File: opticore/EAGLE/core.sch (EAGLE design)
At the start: 121 parts, among them IC1 MCP1825S-3302E, IC2 MC33269T-5.0, J1 POWER_JACKSLT, Q1 MMDT3904, Q2 2N3904, Q3 2N3904, Q4 2N3904, Q5 2N3904, Q6 2N3904, Q7 2N3904, Q8 2N3904, U2 STM32F10XCXT6, U3 SST25VF040B-S2, U4 NL17SZ125SOT553, X1 USB-MICROB, X2 IPEX-20279-001E, Y1 32Khz, Y2 8Mhz

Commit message: Initial placement of relays
Still need to do a lot of work. Placement is temporary.

LEDs and the rest of the components need to be placed.

One problem is that I can't move what they originally did. Option #1: Redo what they did. (not happening) Option #2: Try adding their schematic as a part then placing it on a new shm. Option #3: Try to find a way to move it online.

Signed-off-by: Scott Lerner <scottphiliplerner@gmail.com>
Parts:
- removed Q1: MMDT3904, SparkFun-DiscreteSemi:MMDT3904
- removed U$1: SPARK_LOGO2, Spark:SPARK_LOGO2
- added Q9: 2N3904, transistor-npn:2N3904
- Q2: value 2N3904 -> MMDT3904; device transistor-npn:2N3904 -> SparkFun-DiscreteSemi:MMDT3904
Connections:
- net +3V3: now also Q2G$1.C; no longer Q1G$1.C
- net GND: now also Q2G$2.E, Q9.E; no longer Q1G$2.E, Q2.E
- net N$13: now also Q2G$1.B, Q2G$2.C; no longer Q1G$1.B, Q1G$2.C
- net N$16: now also Q2G$1.E; no longer Q1G$1.E
- net N$18: now also Q3.C; no longer Q2.C
- net N$19: now also Q4.C; no longer Q3.C
- net N$20: now also Q4.B; no longer Q3.B
- net N$22: now also Q6.C; no longer Q4.C
- net N$23: now also Q6.B; no longer Q4.B
- net N$24: now also Q3.B; no longer Q2.B
- net N$26: now also Q7.C; no longer Q5.C
- net N$27: now also Q7.B; no longer Q5.B
- net N$29: now also Q5.C; no longer Q6.C
- net N$30: now also Q5.B; no longer Q6.B
- net N$32: now also Q8.C; no longer Q7.C
- net N$33: now also Q8.B; no longer Q7.B
- net N$35: now also Q9.C; no longer Q8.C
- net N$36: now also Q9.B; no longer Q8.B
- net N$8: now also Q2G$2.B; no longer Q1G$2.B
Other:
- moved on the sheet: Q3, Q4, Q5, Q6, Q7, Q8

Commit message: Close to final revision
I'm working on laying down the final placement as well as the ground
planes. I'll try and work on it soon.
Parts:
- removed ANT1: AT8010, Spark:AT8010
- removed BTN, RESET: KMR211GLFS, Spark:TAC_SWITCHSMD
- removed C1, C2: 4.7uF, rcl:C-EUC0603
- removed C10, C11: 22pF, rcl:C-EUC0603
- removed C12, C13, C14, C16, C3, C6, C7: 100nF, rcl:C-EUC0603
- removed C15: 10uF, Spark:TANT-CAP1206
- removed C4: 2.2pF, rcl:C-EUC0603
- removed C5, C8, C9: 10pF, rcl:C-EUC0603
- removed D8: 1N4004, diode:1N4004
- removed D9: GREEN, SparkFun-LED:LED-GREEN0603
- removed IC1: MCP1825S-3302E, Spark:MCP1825S-SOT223
- removed JP1, JP2: M12PTH, Spark:M12PTH
- removed JP3, JP4, JP5, JP6, JP7, JP8, JP9: (no value), SparkFun-Connectors:M03-SCREW-5MM
- removed L1: 2.2nH, SparkFun-Passives:INDUCTOR0603
- removed L2: Bead, SparkFun-Passives:INDUCTOR0603
- removed LED_RGB: (no value), Spark:TOPLED-3PLCC
- removed LED_USR: (no value), SparkFun:LED0603
- removed LOGO1: OSHW-LOGOS, SparkFun-Aesthetics:OSHW-LOGOS
- removed Q8, Q9: 2N3904, transistor-npn:2N3904
- removed R25, R27, R28, R30: 1K, SparkFun-Passives:RESISTOR0402-RES
- removed R26, R29: 10K, SparkFun-Passives:RESISTOR0402-RES
- removed R31: 1K, SparkFun-Passives:RESISTORAXIAL-0.3
- removed R32, R33: 4.7K, SparkFun-Passives:RESISTOR0402-RES
- removed RN1: EXB-38V102JV, resistor-dil:4R-NEXB38V
- removed STANDOFF1, STANDOFF2, STANDOFF3: STAND-OFF, SparkFun-Electromechanical:STAND-OFF
- removed U1: (no value), CC3000:CC3000
- removed U2: STM32F10XCXT6, stm32:STM32F10XCXT6
- removed U3: SST25VF040B-S2, Spark:SST25VF040B-S2
- removed U4: NL17SZ125SOT553, Spark:NL17SZ125SOT553
- removed X2: IPEX-20279-001E, Spark:IPEX-20279-001E
- removed Y1: 32Khz, Spark:Q_FC135
- removed Y2: 8Mhz, SparkFun-FreqCtrl:CRYSTAL5X3
- added JP11, JP12: M12PTH, Spark:M12PTH
- added LED8: (no value), SparkFun-LED:LED3MM
- added LOGO2: OSHW-LOGOL, SparkFun-Aesthetics:OSHW-LOGOL
- added Q1: 2N3904, transistor-npn:2N3904
- C17, C18, C19: value (none) -> 100uF
- D1: value DIODE -> 1N4004; device Spark:DIODE -> diode:1N4004
- LED1, LED2, LED3, LED4, LED5, LED6, LED7: value RED -> (none); device SparkFun-LED:LED0603 -> SparkFun-LED:LED3MM
- Q2: value MMDT3904 -> 2N3904; device SparkFun-DiscreteSemi:MMDT3904 -> transistor-npn:2N3904
- R1, R8: value 10K -> 1K; device rcl:R-US_R0603 -> SparkFun-Resistors:RESISTORAXIAL-0.3
- R10, R13, R16, R19, R24: device SparkFun-Passives:RESISTOR0402-RES -> SparkFun-Resistors:RESISTORAXIAL-0.3
- R11, R14, R17, R20: value 10K -> 1K; device SparkFun-Passives:RESISTOR0402-RES -> SparkFun-Resistors:RESISTORAXIAL-0.3
- R12, R15, R18, R21: value 1K -> 10K; device SparkFun-Passives:RESISTOR0402-RES -> SparkFun-Resistors:RESISTORAXIAL-0.3
- R2: value 33K -> 1K; device rcl:R-US_R0603 -> SparkFun-Resistors:RESISTORAXIAL-0.3
- R22: value 1K -> 4.7K; device SparkFun-Passives:RESISTOR0402-RES -> SparkFun-Resistors:RESISTORAXIAL-0.3
- R23: value 10K -> 4.7K; device SparkFun-Passives:RESISTOR0402-RES -> SparkFun-Resistors:RESISTORAXIAL-0.3
- R3: value 1K5 -> 10K; device rcl:R-US_R0603 -> SparkFun-Resistors:RESISTORAXIAL-0.3
- R4: device rcl:R-US_R0603 -> SparkFun-Resistors:RESISTORAXIAL-0.3
- R5: value 22 -> 1K; device rcl:R-US_R0603 -> SparkFun-Resistors:RESISTORAXIAL-0.3
- R6: value 22 -> 10K; device rcl:R-US_R0603 -> SparkFun-Resistors:RESISTORAXIAL-0.3
- R7: value 47K -> 1K; device rcl:R-US_R0603 -> SparkFun-Resistors:RESISTORAXIAL-0.3
- R9: value 1K -> 10K; device rcl:R-US_R0603 -> SparkFun-Resistors:RESISTORAXIAL-0.3
- X1: value USB-MICROB -> FFKV8; device Spark:USBUSB-MICROB-SLOT-HOLE -> con-phoenix-508:FFKV8
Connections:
- removed net BTN: BTN.3, U2PORTB_L.PB2
- removed net LED1: LED_USR.A, RN1D.1
- removed net LED2: RN1A.2, U2PORTA_H.PA8
- removed net LED3: RN1B.2, U2PORTA_H.PA9
- removed net LED4: RN1C.2, U2PORTA_H.PA10
- removed net MAIN1: JP3.2, U$2.MAIN
- removed net MAIN2: JP4.2, U$4.MAIN
- removed net MAIN3: JP7.2, U$7.MAIN
- removed net MAIN4: JP5.2, U$5.MAIN
- removed net MAIN5: JP6.2, U$6.MAIN
- removed net MAIN6: JP8.2, U$8.MAIN
- removed net MAIN7: JP9.2, U$9.MAIN
- removed net MEM_CS: R9.1, U2PORTB_H.PB9, U3.CE
- removed net N$10: LED_RGB.CRED, RN1A.1
- removed net N$12: LED_RGB.CBLUE, RN1B.1
- removed net N$13: Q2G$1.B, Q2G$2.C, R1.1, R2.2
- removed net N$14: LED_RGB.CGREEN, RN1C.1
- removed net N$15: U1.SDA_CC3000, U1.SDA_EEPROM
- removed net N$16: Q2G$1.E, R3.2
- removed net N$17: LED2.A, R13.1
- removed net N$21: LED3.A, R16.1
- removed net N$25: LED4.A, R19.1
- removed net N$28: LED5.A, R22.1
- removed net N$31: LED6.A, R25.1
- removed net N$34: LED7.A, R28.1
- removed net N$43: R32.2, SJ1.3
- removed net N$44: R33.2, SJ1.1
- removed net NC1: JP3.3, U$2.NC
- removed net NC2: JP4.3, U$4.NC
- removed net NC3: JP7.3, U$7.NC
- removed net NC4: JP5.3, U$5.NC
- removed net NC5: JP6.3, U$6.NC
- removed net NC6: JP8.3, U$8.NC
- removed net NC7: JP9.3, U$9.NC
- removed net OSC32_IN: C9.1, U2PORTC.PC14, Y1.1
- removed net OSC32_OUT: C8.1, U2PORTC.PC15, Y1.2
- removed net OSC_IN: C11.1, U2PORTD/OSC.PD0/OSC<=, Y2.1
- removed net OSC_OUT: C10.1, U2PORTD/OSC.PD1/OSC=>, Y2.2
- removed net SPI_DOUT: U1.SPI_DOUT, U4.IN
- removed net SPI_MISO: U2PORTB_H.PB14, U3.SO, U4.OUT
- removed net SPI_MOSI: U1.SPI_DIN, U2PORTB_H.PB15, U3.SI
- removed net SPI_SCK: U1.SPI_CLK, U2PORTB_H.PB13, U3.SCK
- removed net USBM: R6.1, U2PORTA_H.PA11
- removed net USBP: R5.1, U2PORTA_H.PA12
- removed net USB_DISC: R4.1, R7.2, U2PORTB_H.PB10
- removed net UVCC: D1.ANODE, R1.2, X1.VBUS
- removed net WIFI_CS: U1.SPI_CS, U2PORTB_H.PB12, U4./OE
- removed net WIFI_EN: U1.VBAT_SW_EN, U2PORTB_H.PB8
- removed net WIFI_INT: U1.SPI_IRQ, U2PORTB_H.PB11
- new net MAIN: U$2.MAIN, U$4.MAIN, U$5.MAIN, U$6.MAIN, U$7.MAIN, U$8.MAIN, U$9.MAIN, X1-8.2
- net !RST: now also JP12.2; no longer C6.2, JP2.2, R8.1, RESET.1, U2RESET.NRST
- net +3V3: now also JP12.1; no longer C12.1, C14.1, C16.1, C2.1, C3.1, C7.1, IC1.OUT, JP2.1, L2.1, LED_RGB.A2, Q2G$1.C, R7.1, R8.2, R9.2, U1.VBAT_IN, U1.VIO_HOST, U2AN_POWER.VBAT, U2POWER.VDD_1, U2POWER.VDD_2, U2POWER.VDD_3, U3.HOLD, U3.VDD, U3.WP, U4.VCC
- net 5V: now also D1.C, R1.2, R24.1, R4.2, R7.2; no longer D8.C, R22.2, R25.2, R28.2, R31.1
- net A2: now also JP11.10; no longer JP1.10, U2PORTA_L.PA4
- net A3: now also JP11.9; no longer JP1.9, U2PORTA_L.PA5
- net A4: now also JP11.8; no longer JP1.8, U2PORTA_L.PA6
- net A5: now also JP11.7; no longer JP1.7, U2PORTA_L.PA7
- net A6: now also JP11.6; no longer JP1.6, U2PORTB_L.PB0
- net A7: now also JP11.5; no longer JP1.5, U2PORTB_L.PB1
- net D7: now also JP12.5; no longer JP2.5, RN1D.2, U2PORTA_H.PA13
- net GND: now also JP11.2, JP12.4, LED8.C, Q1.E, Q2.E, R12.1, R15.1, R18.1, R21.1, R3.1, R6.1, R9.1; no longer BTN.2, C1.2, C10.2, C11.2, C12.2, C13.2, C14.2, C15.-, C16.2, C2.2, C3.2, C6.1, C7.2, C8.2, C9.2, D9.C, IC1.GND@1, IC1.GND@2, JP1.2, JP2.4, L1.2, LED_USR.C, Q2G$2.E, Q8.E, Q9.E, R11.1, R14.1, R17.1, R2.1, R20.1, R23.1, R26.1, R29.1, RESET.4, U1.EXT_32K, U1.GND@1, U1.GND@10, U1.GND@11, U1.GND@16, U1.GND@18, U1.GND@20, U1.GND@22, U1.GND@25, U1.GND@31, U1.GND@32, U1.GND@33, U1.GND@34, U1.GND@36, U1.GND@37, U1.GND@38, U1.GND@39, U1.GND@40, U1.GND@41, U1.GND@42, U1.GND@43, U1.GND@44, U1.GND@45, U1.GND@46, U1.GND@9, U2AN_POWER.VSSA, U2POWER.VSS_1, U2POWER.VSS_2, U2POWER.VSS_3, U2RESET.BOOT0, U3.VSS, U4.GND, X1.GND, X2.GND@1
- net N$1: now also LED1.A, R1.1; no longer R3.1, R5.2, X1.D+
- net N$18: now also D1.A, Q1.C; no longer D2.A, Q3.C
- net N$19: now also D2.A, Q2.C; no longer D3.A, Q4.C
- net N$2: now also LED2.A, R4.1; no longer C5.2, X2.1
- net N$20: now also Q2.B, R5.2, R6.2; no longer Q4.B, R14.2, R15.1
- net N$22: now also D5.A, LED5.C, Q5.C; no longer D4.A, LED3.C, Q6.C
- net N$23: now also Q5.B, R14.2, R15.2; no longer Q6.B, R17.2, R18.1
- net N$24: now also Q1.B, R2.2, R3.2; no longer Q3.B, R11.2, R12.1
- net N$26: now also D6.A, LED6.C, Q6.C; no longer D5.A, LED4.C, Q7.C
- net N$27: now also Q6.B, R17.2, R18.2; no longer Q7.B, R20.2, R21.1
- net N$29: now also D3.A, LED3.C, Q3.C; no longer D6.A, LED5.C, Q5.C
- net N$3: now also LED5.A, R13.1; no longer ANT1.SIGNAL, C4.1, L1.1
- net N$30: now also Q3.B, R8.2, R9.2; no longer Q5.B, R23.2, R24.1
- net N$32: now also LED7.C, Q7.C; no longer LED6.C, Q8.C
- net N$33: now also Q7.B, R20.2, R21.2; no longer Q8.B, R26.2, R27.1
- net N$35: now also D4.A, LED4.C, Q4.C; no longer D8.A, LED7.C, Q9.C
- net N$36: now also Q4.B, R11.2, R12.2; no longer Q9.B, R29.2, R30.1
- net N$39: now also LED8.A, R24.2; no longer D9.A, R31.2
- net N$4: now also LED6.A, R16.1; no longer LED1.A, R10.1
- net N$5: now also LED3.A, R7.1; no longer C4.2, C5.1, U1.RF_ANT
- net N$6: now also LED4.A, R10.1; no longer R6.2, X1.D-
- net N$7: now also LED7.A, R19.1; no longer U1.SCL_CC3000, U1.SCL_EEPROM
- net N$8: now also R22.2, SJ1.3; no longer Q2G$2.B, R4.2
- net N$9: now also R23.2, SJ1.1; no longer U1.WL_EN1, U1.WL_EN2
- net NO1: now also X1-7.2; no longer JP3.1
- net NO2: now also X1-6.2; no longer JP4.1
- net NO3: now also X1-5.2; no longer JP7.1
- net NO4: now also U$9.NO, X1-4.2; no longer JP5.1, U$5.NO
- net NO5: now also U$5.NO, X1-3.2; no longer JP6.1, U$6.NO
- net NO6: now also U$6.NO, X1-2.2; no longer JP8.1, U$8.NO
- net NO7: now also U$8.NO, X1-1.2; no longer JP9.1, U$9.NO
- net RAW: now also JP11.1; no longer C1.1, D1.CATHODE, IC1.IN, JP1.1
- net RELAY1: now also JP12.12, R2.1; no longer JP2.12, R12.2, U2PORTB_L.PB7
- net RELAY2: now also JP12.11, R5.1; no longer JP2.11, R15.2, U2PORTB_L.PB6
- net RELAY3: now also JP12.10, R8.1; no longer JP2.10, R24.2, U2PORTB_L.PB5
- net RELAY4: now also JP12.9, R11.1; no longer JP2.9, R18.2, U2PORTB_L.PB4
- net RELAY5: now also JP12.8, R14.1; no longer JP2.8, R21.2, U2PORTB_L.PB3
- net RELAY6: now also JP12.7, R17.1; no longer JP2.7, R27.2, U2PORTA_H.PA15
- net RELAY7: now also JP12.6, R20.1; no longer JP2.6, R30.2, U2PORTA_H.PA14
- net RX: now also JP11.4; no longer JP1.4, U2PORTA_L.PA3
- net SCL: now also JP11.11, R23.1; no longer JP1.11, R33.1, U2PORTA_L.PA1
- net SDA: now also JP11.12, R22.1; no longer JP1.12, R32.1, U2PORTA_L.PA0
- net TX: now also JP11.3; no longer JP1.3, U2PORTA_L.PA2
- net VDDA: now also JP12.3; no longer C13.1, C15.+, JP2.3, L2.2, U2AN_POWER.VDDA
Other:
- note removed: "Arduino Pro Mini Design by Spark Fun Electronics"
- note removed: "External FLASH"
- note removed: "Max Current Output: 500mA"
- note removed: "Max Voltage Input: 6VDC"
- note removed: "Original Arduino Mini Design by Team Arduino"
- note removed: "Power Regulator"
- note removed: "Pro Micro Design by Spark Fun Electronics"
- note removed: "STM32 Decoupling, Reset, Crystal, & Boot"
- note removed: "STM32 GPIO"
- note removed: "STM32 Power"
- note removed: "Spark Core"
- note removed: "Spark Core Design by Spark Devices"
- note removed: "USB"
- note removed: "VCC = 3.3V Output"
- note removed: "VDDA"
- note removed: "Wi-Fi Module"
- moved on the sheet: C17, C18, C19, C20, C21, D2, D3, D4, D5, D6, D7, IC2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

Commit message: Stuff I did on the plane to PHL
Most just moving some stuff around and laying down traces.

Signed-off-by: Scott Lerner <scottphiliplerner@gmail.com>
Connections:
- net GND: now also U$2.NC, U$4.NC, U$5.NC, U$6.NC, U$7.NC, U$8.NC, U$9.NC
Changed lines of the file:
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@@
 </classes>
 <parts>
-<part name="FRAME3" library="SparkFun" deviceset="FRAME-LETTER" device=""/>
+<part name="FRAME1" library="SparkFun" deviceset="FRAME-LETTER" device=""/>
 <part name="U$2" library="SparkFun-Electromechanical" deviceset="RELAY" device="PTH4"/>
 <part name="U$3" library="SparkFun-Sensors" deviceset="BMP085" device=""/>
@@
 </plain>
 <instances>
-<instance part="FRAME3" gate="G$1" x="0" y="0"/>
-<instance part="FRAME3" gate="G$2" x="147.32" y="0"/>
+<instance part="FRAME1" gate="G$1" x="0" y="0"/>
+<instance part="FRAME1" gate="G$2" x="147.32" y="0"/>
 <instance part="U$2" gate="G$1" x="35.56" y="152.4"/>
 <instance part="U$3" gate="G$1" x="210.82" y="88.9"/>
@@
 <instance part="X1" gate="-7" x="233.68" y="137.16" rot="MR0"/>
 <instance part="X1" gate="-8" x="233.68" y="132.08" rot="MR0"/>
-<instance part="LOGO2" gate="G$1" x="187.96" y="48.26"/>
+<instance part="LOGO2" gate="G$1" x="185.42" y="48.26"/>
 <instance part="R1" gate="G$1" x="10.16" y="162.56" rot="R90"/>
 <instance part="R2" gate="G$1" x="25.4" y="134.62"/>
@@
 <pinref part="R21" gate="G$1" pin="1"/>
 </segment>
+<segment>
+<pinref part="U$2" gate="G$1" pin="NC"/>
+<wire x1="43.18" y1="157.48" x2="50.8" y2="157.48" width="0.1524" layer="91"/>
+<label x="43.18" y="157.48" size="1.778" layer="95"/>
+</segment>
+<segment>
+<pinref part="U$4" gate="G$1" pin="NC"/>
+<wire x1="93.98" y1="157.48" x2="101.6" y2="157.48" width="0.1524" layer="91"/>
+<label x="93.98" y="157.48" size="1.778" layer="95"/>
+</segment>
+<segment>
+<pinref part="U$7" gate="G$1" pin="NC"/>
+<wire x1="144.78" y1="157.48" x2="152.4" y2="157.48" width="0.1524" layer="91"/>
+<label x="144.78" y="157.48" size="1.778" layer="95"/>
+</segment>
+<segment>
+<pinref part="U$9" gate="G$1" pin="NC"/>
+<wire x1="198.12" y1="157.48" x2="205.74" y2="157.48" width="0.1524" layer="91"/>
+<label x="198.12" y="157.48" size="1.778" layer="95"/>
+</segment>
+<segment>
+<pinref part="U$8" gate="G$1" pin="NC"/>
+<wire x1="144.78" y1="96.52" x2="152.4" y2="96.52" width="0.1524" layer="91"/>
+<label x="144.78" y="96.52" size="1.778" layer="95"/>
+</segment>
+<segment>
+<pinref part="U$6" gate="G$1" pin="NC"/>
+<wire x1="93.98" y1="96.52" x2="101.6" y2="96.52" width="0.1524" layer="91"/>
+<label x="93.98" y="96.52" size="1.778" layer="95"/>
+</segment>
+<segment>
+<pinref part="U$5" gate="G$1" pin="NC"/>
+<wire x1="43.18" y1="96.52" x2="50.8" y2="96.52" width="0.1524" layer="91"/>
+<label x="43.18" y="96.52" size="1.778" layer="95"/>
+</segment>
 </net>

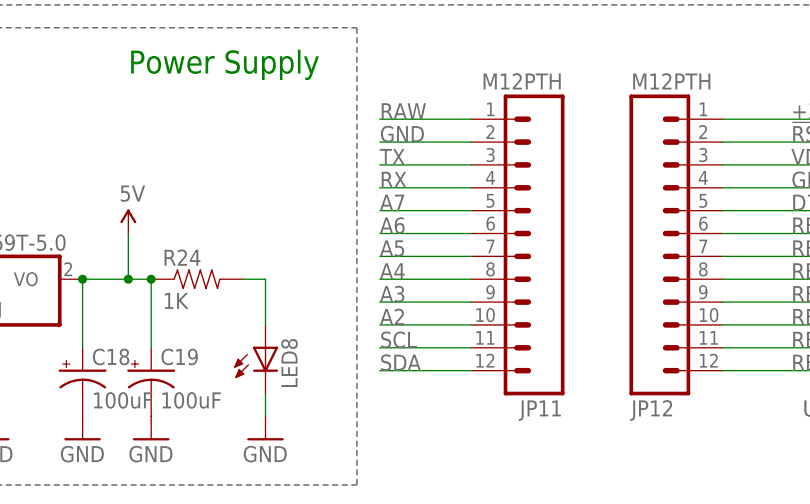
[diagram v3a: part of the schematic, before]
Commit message: More routing
Slowly getting closer to 'optimal', but that pressure sensor is
annoying.
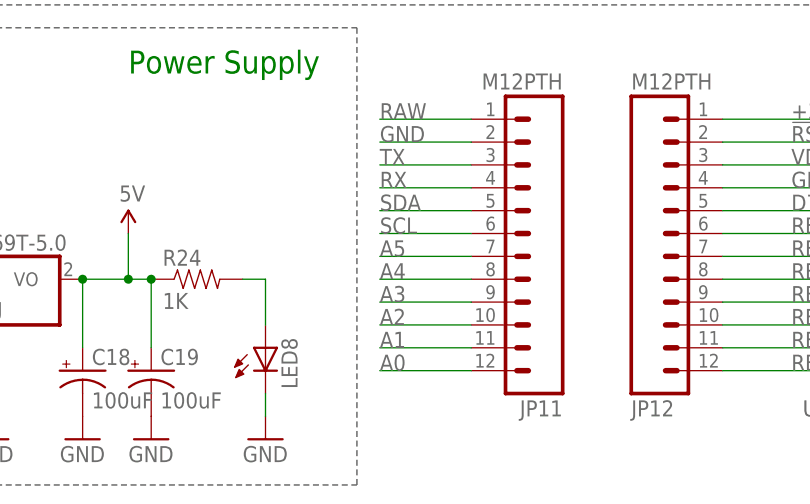
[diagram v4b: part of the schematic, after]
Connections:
- removed net A6: JP11.6
- removed net A7: JP11.5
- new net A0: JP11.12
- new net A1: JP11.11
- net SCL: now also JP11.6; no longer JP11.11
- net SDA: now also JP11.5; no longer JP11.12
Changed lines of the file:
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@@
-</segment>
-</net>
-<net name="A6" class="0">
-<segment>
-<wire x1="99.06" y1="30.48" x2="88.9" y2="30.48" width="0.1524" layer="91"/>
-<label x="88.9" y="30.48" size="1.778" layer="95"/>
-<pinref part="JP11" gate="G$1" pin="6"/>
-</segment>
-</net>
-<net name="A7" class="0">
-<segment>
-<wire x1="99.06" y1="33.02" x2="88.9" y2="33.02" width="0.1524" layer="91"/>
-<label x="88.9" y="33.02" size="1.778" layer="95"/>
-<pinref part="JP11" gate="G$1" pin="5"/>
 </segment>
 </net>
@@
 </segment>
 <segment>
-<wire x1="99.06" y1="15.24" x2="88.9" y2="15.24" width="0.1524" layer="91"/>
-<label x="88.9" y="15.24" size="1.778" layer="95"/>
-<pinref part="JP11" gate="G$1" pin="12"/>
+<wire x1="99.06" y1="33.02" x2="88.9" y2="33.02" width="0.1524" layer="91"/>
+<label x="88.9" y="33.02" size="1.778" layer="95"/>
+<pinref part="JP11" gate="G$1" pin="5"/>
 </segment>
 </net>
@@
 </segment>
 <segment>
+<wire x1="99.06" y1="30.48" x2="88.9" y2="30.48" width="0.1524" layer="91"/>
+<label x="88.9" y="30.48" size="1.778" layer="95"/>
+<pinref part="JP11" gate="G$1" pin="6"/>
+</segment>
+</net>
+<net name="N$8" class="0">
+<segment>
+<pinref part="SJ1" gate="G$1" pin="3"/>
+<pinref part="R22" gate="G$1" pin="2"/>
+</segment>
+</net>
+<net name="N$9" class="0">
+<segment>
+<pinref part="SJ1" gate="G$1" pin="1"/>
+<pinref part="R23" gate="G$1" pin="2"/>
+</segment>
+</net>
+<net name="N$1" class="0">
+<segment>
+<pinref part="R1" gate="G$1" pin="1"/>
+<pinref part="LED1" gate="G$1" pin="A"/>
+</segment>
+</net>
+<net name="N$2" class="0">
+<segment>
+<pinref part="R4" gate="G$1" pin="1"/>
+<pinref part="LED2" gate="G$1" pin="A"/>
+</segment>
+</net>
+<net name="N$3" class="0">
+<segment>
+<pinref part="R13" gate="G$1" pin="1"/>
+<pinref part="LED5" gate="G$1" pin="A"/>
+</segment>
+</net>
+<net name="N$4" class="0">
+<segment>
+<pinref part="R16" gate="G$1" pin="1"/>
+<pinref part="LED6" gate="G$1" pin="A"/>
+</segment>
+</net>
+<net name="N$5" class="0">
+<segment>
+<pinref part="R7" gate="G$1" pin="1"/>
+<pinref part="LED3" gate="G$1" pin="A"/>
+</segment>
+</net>
+<net name="N$6" class="0">
+<segment>
+<pinref part="R10" gate="G$1" pin="1"/>
+<pinref part="LED4" gate="G$1" pin="A"/>
+</segment>
+</net>
+<net name="N$7" class="0">
+<segment>
+<pinref part="R19" gate="G$1" pin="1"/>
+<pinref part="LED7" gate="G$1" pin="A"/>
+</segment>
+</net>
+<net name="A1" class="0">
+<segment>
 <wire x1="99.06" y1="17.78" x2="88.9" y2="17.78" width="0.1524" layer="91"/>
 <label x="88.9" y="17.78" size="1.778" layer="95"/>
@@
 </segment>
 </net>
-<net name="N$8" class="0">
-<segment>
-<pinref part="SJ1" gate="G$1" pin="3"/>
-<pinref part="R22" gate="G$1" pin="2"/>
-</segment>
-</net>
-<net name="N$9" class="0">
-<segment>
-<pinref part="SJ1" gate="G$1" pin="1"/>
-<pinref part="R23" gate="G$1" pin="2"/>
-</segment>
-</net>
-<net name="N$1" class="0">
-<segment>
-<pinref part="R1" gate="G$1" pin="1"/>
-<pinref part="LED1" gate="G$1" pin="A"/>
-</segment>
-</net>
-<net name="N$2" class="0">
-<segment>
-<pinref part="R4" gate="G$1" pin="1"/>
-<pinref part="LED2" gate="G$1" pin="A"/>
-</segment>
-</net>
-<net name="N$3" class="0">
-<segment>
-<pinref part="R13" gate="G$1" pin="1"/>
-<pinref part="LED5" gate="G$1" pin="A"/>
-</segment>
-</net>
-<net name="N$4" class="0">
-<segment>
-<pinref part="R16" gate="G$1" pin="1"/>
-<pinref part="LED6" gate="G$1" pin="A"/>
-</segment>
-</net>
-<net name="N$5" class="0">
-<segment>
-<pinref part="R7" gate="G$1" pin="1"/>
-<pinref part="LED3" gate="G$1" pin="A"/>
-</segment>
-</net>
-<net name="N$6" class="0">
-<segment>
-<pinref part="R10" gate="G$1" pin="1"/>
-<pinref part="LED4" gate="G$1" pin="A"/>
-</segment>
-</net>
-<net name="N$7" class="0">
-<segment>
-<pinref part="R19" gate="G$1" pin="1"/>
-<pinref part="LED7" gate="G$1" pin="A"/>
-</segment>
-</net>
+<net name="A0" class="0">
+<segment>
+<wire x1="99.06" y1="15.24" x2="88.9" y2="15.24" width="0.1524" layer="91"/>
+<label x="88.9" y="15.24" size="1.778" layer="95"/>
+<pinref part="JP11" gate="G$1" pin="12"/>
+</segment>
+</net>

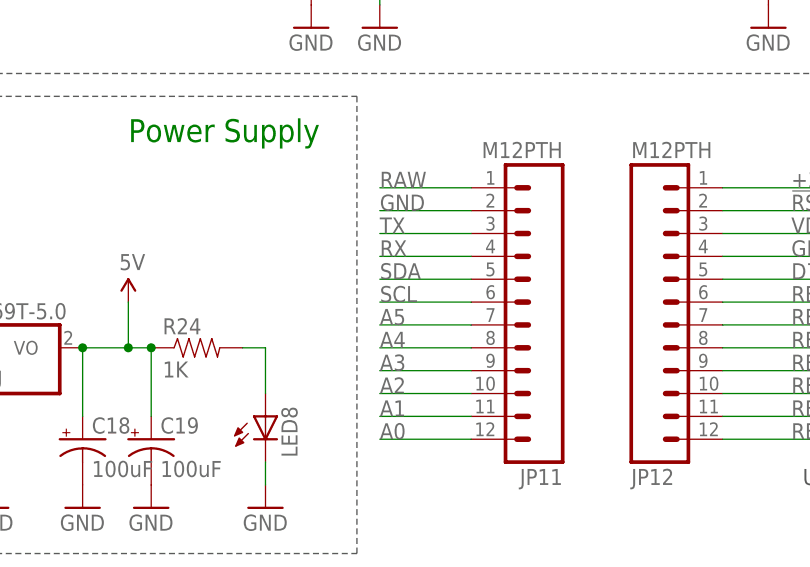
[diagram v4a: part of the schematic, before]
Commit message: Initial Final Draft
At this point, I have done a decent amount of routing, re-routing, and replacement. I am fairly confident that everything will work. I would still want to do another run through for bug fixes though. Creating separate branch for that.

Signed-off-by: Scott Lerner <scottphiliplerner@gmail.com>
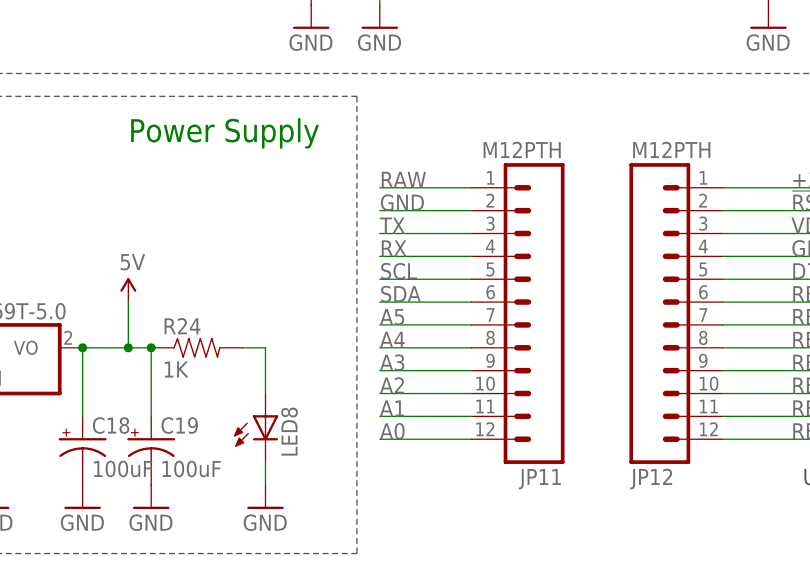
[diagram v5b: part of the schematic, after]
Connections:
- net SCL: now also JP11.5; no longer JP11.6
- net SDA: now also JP11.6; no longer JP11.5
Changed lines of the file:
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@@
 </segment>
 <segment>
-<wire x1="99.06" y1="33.02" x2="88.9" y2="33.02" width="0.1524" layer="91"/>
-<label x="88.9" y="33.02" size="1.778" layer="95"/>
-<pinref part="JP11" gate="G$1" pin="5"/>
+<wire x1="99.06" y1="30.48" x2="88.9" y2="30.48" width="0.1524" layer="91"/>
+<label x="88.9" y="30.48" size="1.778" layer="95"/>
+<pinref part="JP11" gate="G$1" pin="6"/>
 </segment>
 </net>
@@
 </segment>
 <segment>
-<wire x1="99.06" y1="30.48" x2="88.9" y2="30.48" width="0.1524" layer="91"/>
-<label x="88.9" y="30.48" size="1.778" layer="95"/>
-<pinref part="JP11" gate="G$1" pin="6"/>
+<wire x1="99.06" y1="33.02" x2="88.9" y2="33.02" width="0.1524" layer="91"/>
+<label x="88.9" y="33.02" size="1.778" layer="95"/>
+<pinref part="JP11" gate="G$1" pin="5"/>
 </segment>
 </net>
@@
 </sheet>
 </sheets>
+<errors>
+</errors>
 </schematic>
 </drawing>
